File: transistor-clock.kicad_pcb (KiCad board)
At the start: 2 copper layers, 98 parts, among them J1 Screw_Terminal_01x02, J10 Conn_01x10_Socket, J11 Conn_01x06_Socket, J12 Conn_01x10_Socket, J13 Conn_01x03_Socket, J2 Conn_01x01_Socket, J3 Conn_01x01_Socket, J4 Conn_01x01_Socket, J5 Conn_01x01_Socket, J6 Conn_01x01_Socket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

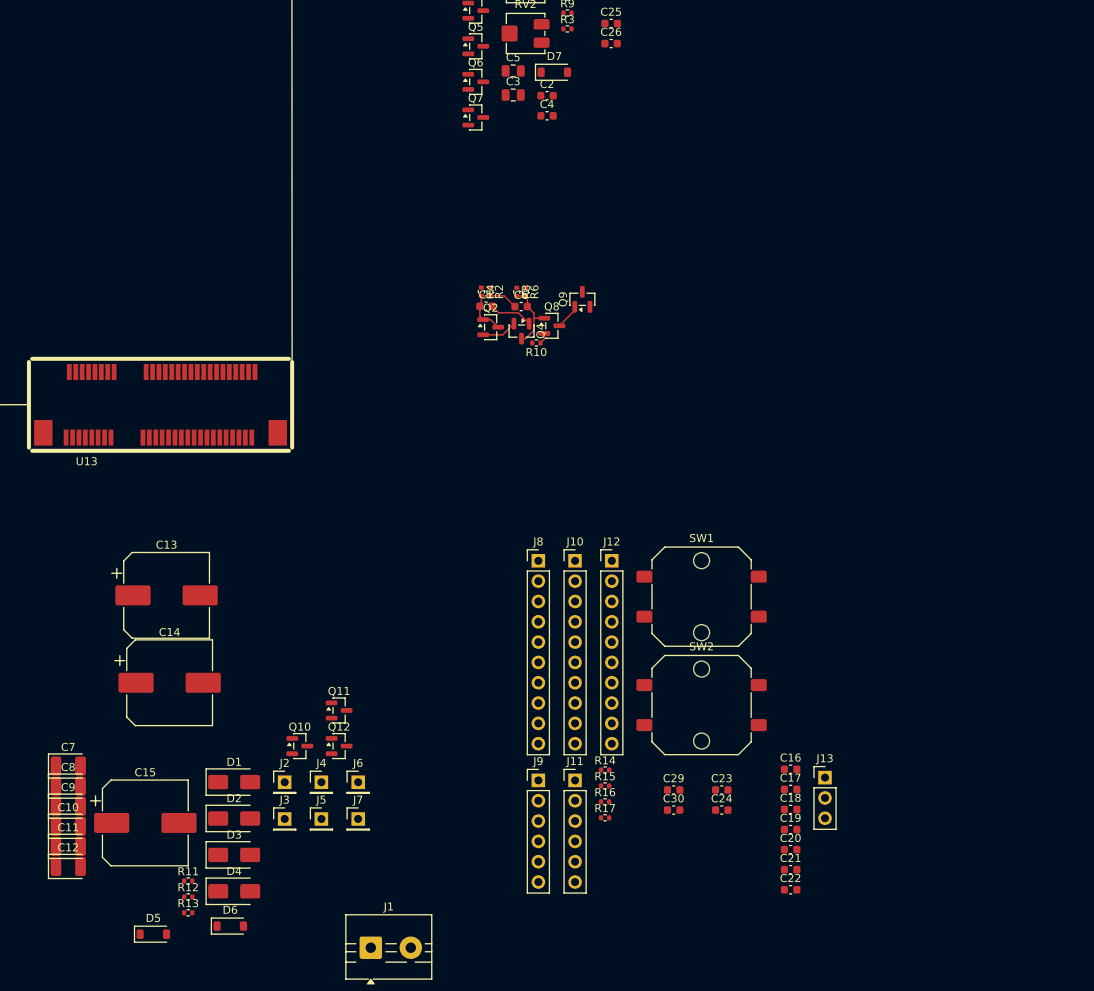
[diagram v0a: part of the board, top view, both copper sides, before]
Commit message: added module for PSU
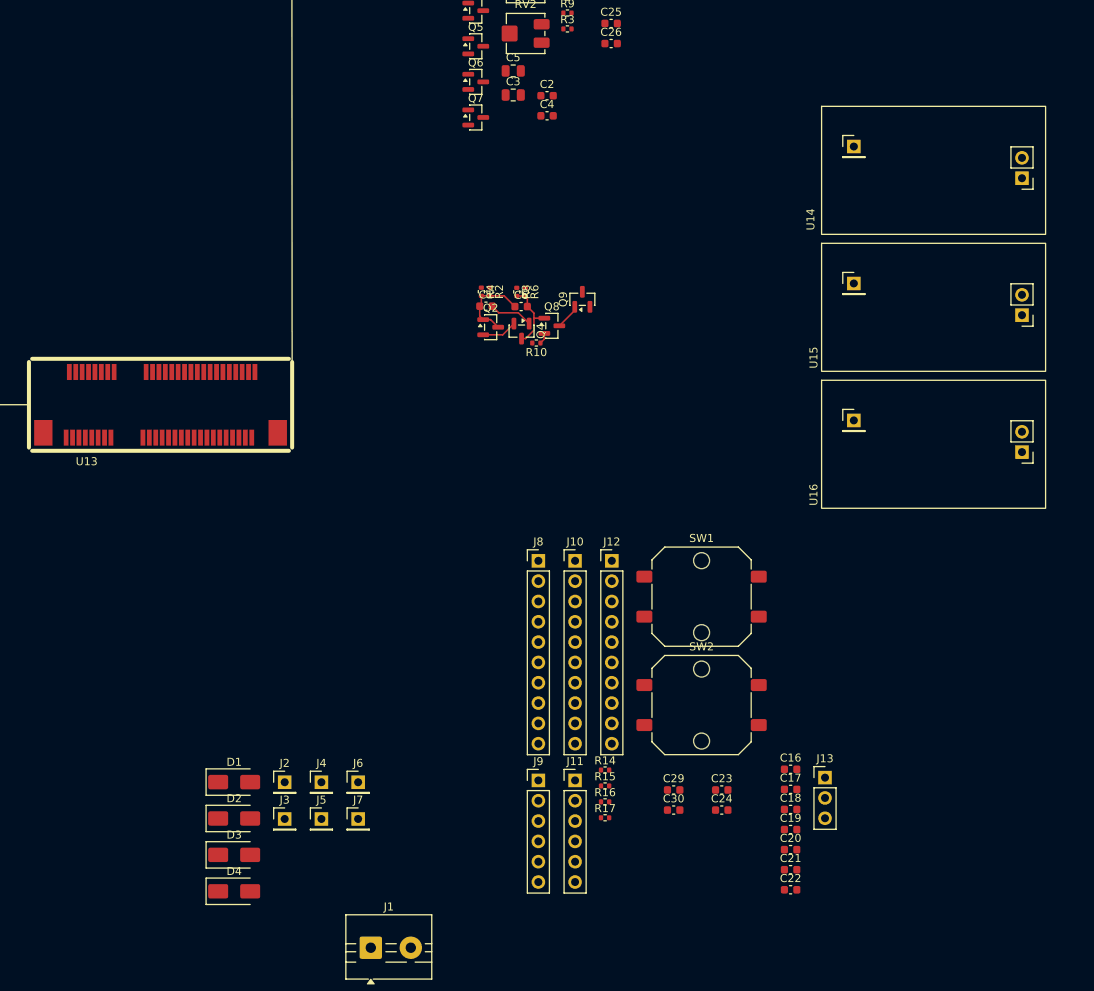
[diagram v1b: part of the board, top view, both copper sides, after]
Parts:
- removed C10, C11, C12, C7, C8, C9: 100u, Capacitor_Tantalum_SMD:CP_EIA-3528-12_Kemet-T
- removed C13, C14, C15: 1000u, Capacitor_SMD:CP_Elec_10x10.5
- removed D5: 3V9, Diode_SMD:D_SOD-123
- removed D6, D7: 13V, Diode_SMD:D_SOD-123
- removed Q10, Q11, Q12: MMBT3904, Package_TO_SOT_SMD:SOT-23
- removed R11, R12, R13: 560, Resistor_SMD:R_0402_1005Metric
- added U14: 3V3, custom:module_PSU, F.Cu at (404.7, 281.4)
- added U15: 12V, custom:module_PSU, F.Cu at (404.7, 298.5)
- added U16: -12V, custom:module_PSU, F.Cu at (404.7, 315.6)
- U1, U2, U3: value ~ -> SSR
- U10, U4, U5, U6, U7: value ~ -> flipflop
- U11, U12, U13, U8, U9: value ~ -> bin-to-dec
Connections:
- D2 pad 1: VSS -> Net-(D2-K)
- D4 pad 2: VSS -> Net-(D2-K)

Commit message: some routing on main board
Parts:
- added TP1: TestPoint_2Pole, Connector_PinHeader_2.54mm:PinHeader_1x02_P2.54mm_Vertical, F.Cu at (78.3, 506.9)
- added TR1: DST-6-36, custom:DST-6-36, F.Cu at (41.3, 350.9)
- added TR2: CL2-20-12, custom:CL2-20-12, F.Cu at (103.0, 350.8)
- R1, R10, R14, R15, R16, R17, R2, R3, R4, R5, R6, R7, R8, R9: footprint Resistor_SMD:R_0402_1005Metric -> Resistor_SMD:R_0603_1608Metric
- SW1: value SW_Push -> MIN +; footprint Button_Switch_SMD:SW_Push_1P1T_NO_CK_PTS125Sx43PSMTR -> Button_Switch_SMD:SW_SPST_EVQPE1
- SW2: value SW_Push -> HR +; footprint Button_Switch_SMD:SW_Push_1P1T_NO_CK_PTS125Sx43PSMTR -> Button_Switch_SMD:SW_SPST_EVQPE1
- moved C27 698.8 mm to (362.8, 437.4)
- moved C28 698.8 mm to (362.8, 439.9)
- moved U14 389.9 mm to (28.9, 385.4)
- moved U4 374.7 mm to (365.0, 502.6)
- moved R1 372.9 mm to (71.3, 495.1), turned to 90 degrees
- moved R5 368.9 mm to (70.8, 486.0), turned to 90 degrees
- moved C29 366.8 mm to (14.0, 437.8)
- moved C30 366.8 mm to (14.0, 440.3)
- moved R3 366.3 mm to (70.8, 489.8), turned to -90 degrees
- moved RV1 366.1 mm to (75.8, 496.2), turned to 180 degrees
- moved R9 362.6 mm to (80.3, 493.7), turned to -90 degrees
- moved R7 362.3 mm to (71.8, 480.6), turned to -90 degrees
- moved C2 357.9 mm to (72.4, 489.8), turned to 90 degrees
- moved Q1 356.8 mm to (77.2, 489.8), turned to 90 degrees
- moved U15 355.8 mm to (59.7, 385.4)
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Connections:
- C2 pad 1: Net-(Q1-B) -> Net-(Q1-C)
- C3 pad 1: Net-(Q1-B) -> Net-(Q1-C)
- Q1 pad 3: Net-(Q1-B) -> Net-(Q1-C)
- R1 pad 2: Net-(Q1-B) -> Net-(Q1-C)
- R3 pad 2: Net-(Q1-B) -> Net-(Q1-C)
- U8 pad 34: /counters/BCD_s0/Q1 -> /counters/BCD_m1/Q2
- U8 pad 36: /counters/BCD_s0/Q3 -> /counters/BCD_m1/Q1
- U8 pad 38: /counters/BCD_s0/Q3 -> /counters/BCD_m1/Q1
- U9 pad 12: /counters/BCD_m1/Q2 -> /counters/BCD_s1/Q2
- U9 pad 14: /counters/BCD_m1/Q1 -> /counters/BCD_s1/Q1
- U9 pad 16: /counters/BCD_m1/Q1 -> /counters/BCD_s1/Q1
- U9 pad 26: /counters/BCD_s1/Q2 -> /counters/BCD_s0/Q1
- U9 pad 28: /counters/BCD_s1/Q1 -> /counters/BCD_s0/Q3
- U9 pad 30: /counters/BCD_s1/Q1 -> /counters/BCD_s0/Q3
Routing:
- net /counters/BCD_h1/Q0: track 0.00 -> 496.8 mm, vias 0 -> 5
- net /counters/BCD_h0/Clr: track 0.00 -> 468.5 mm, vias 0 -> 4
- net /counters/BCD_h1/Clr: track 0.00 -> 360.6 mm, vias 0 -> 2
- net /counters/BCD_h0/Q3: track 0.00 -> 288.2 mm, vias 0 -> 5
- net /counters/BCD_h0/Q1: track 0.00 -> 244.5 mm, vias 0 -> 12
- net /counters/BCD_s0/Q1: track 0.00 -> 238.1 mm, vias 0 -> 14
- net /counters/BCD_m0/Q1: track 0.00 -> 231.8 mm, vias 0 -> 11
- net /counters/BCD_s0/Q0: track 0.00 -> 197.6 mm, vias 0 -> 12
- net /counters/BCD_s0/Q3: track 0.00 -> 197.6 mm, vias 0 -> 6
- net /counters/BCD_m0/Q0: track 0.00 -> 192.8 mm, vias 0 -> 12
- net /counters/BCD_m0/Q3: track 0.00 -> 182.1 mm, vias 0 -> 6
- net /Clk: track 0.00 -> 178.1 mm
- net /counters/BCD_h0/\Q0: track 0.00 -> 178.0 mm, vias 0 -> 12
- net /counters/BCD_s0/\Q0: track 0.00 -> 173.8 mm, vias 0 -> 10
- net /counters/BCD_m0/\Q0: track 0.00 -> 173.8 mm, vias 0 -> 10
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
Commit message: routy mcRouteface
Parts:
- TR1: value DST-6-36 -> Val**
- TR2: value CL2-20-12 -> Val**
- moved U7 447.1 mm to (419.5, 292.1), turned to 180 degrees
- moved J1 425.9 mm to (435.7, 474.3), turned to 180 degrees
- moved C30 425.3 mm to (430.5, 354.4), turned to 180 degrees
- moved C29 424.3 mm to (430.5, 356.9), turned to 180 degrees
- moved C22 423.1 mm to (40.1, 289.8), turned to 180 degrees
- moved U13 414.9 mm to (429.5, 388.6), turned to 90 degrees
- moved U14 387.4 mm to (415.6, 409.3), turned to 180 degrees
- moved C18 381.3 mm to (379.6, 289.7), turned to 180 degrees
- moved TR1 373.6 mm to (403.2, 443.8), turned to 90 degrees
- moved TP1 361.8 mm to (366.2, 287.8), turned to 90 degrees
- moved R1 359.6 mm to (373.2, 299.6), turned to -90 degrees
- moved R3 354.9 mm to (373.8, 304.9), turned to 90 degrees
- moved U4 354.7 mm to (79.5, 292.1), turned to 180 degrees
- moved RV1 353.5 mm to (368.7, 298.5), turned to 0 degrees
- moved C2 352.2 mm to (372.1, 304.9), turned to -90 degrees
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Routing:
- net Net-(U3-Pad12): track 0.00 -> 314.2 mm, vias 0 -> 3
- net Net-(R15-Pad1): track 16.6 -> 287.8 mm
- net Net-(R17-Pad1): track 17.1 -> 275.5 mm
- net /Sqr1: track 0.00 -> 248.0 mm
- net /counters/BDC_s0/8: track 5.53 -> 229.9 mm, vias 0 -> 3
- net /counters/BDC_s0/9: track 0.00 -> 219.5 mm, vias 0 -> 3
- net /counters/BDC_s0/7: track 14.8 -> 218.3 mm, vias 0 -> 2
- net +3V3: track 0.00 -> 203.5 mm, vias 0 -> 69
- net /counters/BDC_s0/4: track 26.3 -> 224.2 mm, vias 0 -> 1
- net /counters/BDC_s0/3: track 22.8 -> 218.2 mm, vias 0 -> 1
- net /counters/BDC_s0/2: track 19.6 -> 214.9 mm, vias 0 -> 1
- net /counters/BDC_s0/5: track 23.4 -> 218.0 mm, vias 0 -> 1
- net /counters/BDC_s0/6: track 19.2 -> 213.0 mm, vias 0 -> 1
- net /counters/BDC_s0/1: track 19.6 -> 206.7 mm, vias 0 -> 1
- net /counters/BDC_s0/0: track 11.9 -> 196.4 mm, vias 0 -> 1
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- added copper zone on B.Cu, net +3V3
- added copper zone on F.Cu, net GND
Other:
- board outline added: 430 x 210 mm

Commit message: routing
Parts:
- TR1: value Val** -> DST-6-36
- TR2: value Val** -> CL2-20-12
- moved U14 93.7 mm to (322.0, 412.3), turned to 90 degrees
- moved Q2 87.7 mm to (406.7, 403.5), turned to 180 degrees
- moved C1 85.7 mm to (407.3, 406.1), turned to 180 degrees
- moved Q4 84.4 mm to (402.9, 403.0), turned to 90 degrees
- moved R4 84.3 mm to (408.2, 408.6), turned to 90 degrees
- moved R10 84.3 mm to (400.6, 401.2), turned to 0 degrees
- moved R2 82.3 mm to (406.4, 408.6), turned to 90 degrees
- moved C6 81.3 mm to (402.9, 406.1), turned to 180 degrees
- moved Q8 80.2 mm to (399.1, 403.7), turned to 180 degrees
- moved U16 79.9 mm to (425.4, 407.9), turned to 0 degrees
- moved R8 79.7 mm to (403.8, 408.6), turned to 90 degrees
- moved R6 77.8 mm to (401.9, 408.6), turned to 90 degrees
- moved Q7 76.8 mm to (394.4, 408.6)
- moved Q9 76.8 mm to (399.0, 407.5)
- moved U3 63.9 mm to (51.4, 414.7), turned to 180 degrees
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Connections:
- TR2 pad 12: VSS -> Net-(Q9-E)
- TR2 pad 7: Net-(Q9-E) -> VSS
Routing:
- net /Sqr2: track 0.00 -> 364.3 mm
- net GND: track 63.0 -> 346.2 mm
- net /counters/relays_s0/Out3: track 0.00 -> 186.7 mm, vias 0 -> 1
- net /counters/relays_s0/Out2: track 0.00 -> 186.1 mm, vias 0 -> 1
- net /counters/relays_s0/Out1: track 0.00 -> 184.7 mm, vias 0 -> 1
- net /counters/relays_s0/Out0: track 0.00 -> 177.0 mm
- net /counters/relays_s0/Out7: track 0.00 -> 176.7 mm, vias 0 -> 1
- net /counters/relays_s0/Out4: track 0.00 -> 176.6 mm, vias 0 -> 1
- net /counters/relays_s0/Out8: track 0.00 -> 176.5 mm, vias 0 -> 1
- net /counters/relays_s0/Out5: track 0.00 -> 176.5 mm, vias 0 -> 1
- net /counters/relays_s0/Out6: track 0.00 -> 175.8 mm, vias 0 -> 1
- net /counters/relays_s0/Out9: track 0.00 -> 172.7 mm
- net VSS: track 51.5 -> 178.7 mm, vias 0 -> 2
- net /counters/relays_s1/Out5: track 0.00 -> 123.6 mm
- net /counters/relays_s1/Out3: track 0.00 -> 123.2 mm
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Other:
- board size 430 x 210 mm -> 430 x 170 mm

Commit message: flipflop wip
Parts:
- added F1: 250mA?, Fuse:Fuse_Littelfuse-NANO2-885, F.Cu at (398.9, 437.6)
- added F2: 2A?, Fuse:Fuse_Littelfuse-NANO2-885, F.Cu at (332.1, 396.5)
- added F3: 250mA?, Fuse:Fuse_Littelfuse-NANO2-885, F.Cu at (405.8, 423.0)
- added F4: 250mA?, Fuse:Fuse_Littelfuse-NANO2-885, F.Cu at (396.7, 423.0)
- added H1: MountingHole, MountingHole:MountingHole_4.3mm_M4_DIN965, F.Cu at (15.0, 285.0)
- added H2: MountingHole, MountingHole:MountingHole_4.3mm_M4_DIN965, F.Cu at (435.0, 285.0)
- added H3: MountingHole, MountingHole:MountingHole_4.3mm_M4_DIN965, F.Cu at (15.0, 447.0)
- added H4: MountingHole, MountingHole:MountingHole_4.3mm_M4_DIN965, F.Cu at (435.0, 447.0)
- added H5: MountingHole, MountingHole:MountingHole_4.3mm_M4_DIN965, F.Cu at (194.0, 335.0)
- added H6: MountingHole, MountingHole:MountingHole_4.3mm_M4_DIN965, F.Cu at (275.0, 335.0)
- moved D2 68.9 mm to (327.1, 434.7), turned to 90 degrees
- moved D1 61.8 mm to (332.9, 432.7), turned to 0 degrees
- moved D4 60.2 mm to (332.9, 436.7), turned to 180 degrees
- moved D3 53.0 mm to (338.9, 434.7), turned to -90 degrees
- moved J10 14.1 mm to (272.3, 445.0)
- moved J11 14.1 mm to (195.5, 445.0)
- moved J12 14.1 mm to (128.9, 445.0)
- moved J13 14.1 mm to (48.4, 445.0)
- moved J2 14.1 mm to (45.8, 450.0)
- moved J3 14.1 mm to (117.5, 450.0)
- moved J4 14.1 mm to (189.2, 450.0)
- moved J5 14.1 mm to (260.8, 450.0)
- moved J6 14.1 mm to (332.5, 450.0)
- moved J7 14.1 mm to (404.1, 450.0)
- moved J8 14.1 mm to (415.6, 445.0)
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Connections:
- net Net-(J1-Pin_1) renamed /AC_N
- net Net-(J13-Pin_1) renamed /counters/relays_h1/Out0
- net Net-(J13-Pin_2) renamed /counters/relays_h1/Out1
- net Net-(J13-Pin_3) renamed /counters/relays_h1/Out2
- TR1 pad 4: Net-(J1-Pin_2) -> /AC_L
- U14 pad 2: +3V3 -> Net-(U14-VCC)
- U15 pad 2: VDD -> Net-(U15-VCC)
- U16 pad 3: VSS -> Net-(U16-GND)
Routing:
- net Net-(J1-Pin_2): track 113.9 -> 27.3 mm
- net Net-(D2-K): track 42.1 -> 127.6 mm
- net Net-(D1-K): track 24.2 -> 87.0 mm, vias 0 -> 1
- net /AC_L: track 0.00 -> 60.0 mm
- net Net-(D3-A): track 40.1 -> 98.3 mm, vias 1 -> 0
- net Net-(U15-VCC): track 0.00 -> 47.6 mm
- net Net-(U16-GND): track 0.00 -> 42.9 mm
- net /counters/relays_m0/Out6: track 112.3 -> 143.0 mm
- net VDD: track 48.7 -> 21.9 mm
- net /counters/relays_h0/Out6: track 51.6 -> 73.9 mm
- net /counters/BDC_s1/5: track 178.5 -> 200.5 mm
- net /counters/relays_h0/Out5: track 51.6 -> 73.2 mm
- net /counters/relays_h0/Out7: track 51.6 -> 73.0 mm
- net /counters/relays_m1/Out3: track 61.0 -> 81.9 mm
- net /counters/relays_m1/Out2: track 61.0 -> 81.7 mm
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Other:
- board size 430 x 170 mm -> 430 x 172 mm

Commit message: updated production files
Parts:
- moved SW1 144.8 mm to (25.8, 447.6)
- moved SW2 144.8 mm to (25.7, 439.1)
- moved R7 33.3 mm to (358.9, 283.8), turned to 180 degrees
- moved R1 33.0 mm to (344.4, 283.3), turned to 0 degrees
- moved R5 33.0 mm to (353.5, 282.7), turned to 0 degrees
- moved R3 32.7 mm to (349.8, 282.7), turned to 180 degrees
- moved C4 30.7 mm to (353.5, 284.3), turned to 0 degrees
- moved C2 30.4 mm to (349.8, 284.3), turned to 0 degrees
- moved RV2 28.2 mm to (359.9, 288.1), turned to 90 degrees
- moved C5 28.0 mm to (353.6, 286.2), turned to 0 degrees
- moved C3 27.7 mm to (349.7, 286.2), turned to 0 degrees
- moved RV1 27.6 mm to (343.3, 287.7), turned to 90 degrees
- moved Q5 25.3 mm to (373.1, 287.9), turned to 0 degrees
- moved Q3 23.7 mm to (353.6, 289.3), turned to -90 degrees
- moved Q1 23.6 mm to (349.7, 289.1), turned to 0 degrees
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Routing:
- net Net-(R15-Pad1): track 287.8 -> 419.0 mm
- net Net-(R17-Pad1): track 275.5 -> 405.6 mm
- net GND: track 332.2 -> 378.7 mm
- net /Clk: track 167.1 -> 182.2 mm
- net Net-(Q3-C): track 20.7 -> 35.7 mm
- net Net-(C17-Pad1): track 121.1 -> 128.2 mm
- net Net-(C16-Pad1): track 144.5 -> 151.6 mm

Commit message: cleanup and DRC
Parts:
- added TP2: TestPoint_2Pole, Connector_PinHeader_2.54mm:PinHeader_1x02_P2.54mm_Vertical, F.Cu at (391.8, 405.1)
- moved H5 59.5 mm to (180.8, 393.0)
- moved H6 58.7 mm to (265.8, 393.0)
- moved C25 22.4 mm to (98.6, 348.1)
- moved C32 22.3 mm to (268.9, 350.7)
- moved C23 22.3 mm to (183.9, 348.1)
- moved C29 21.1 mm to (353.6, 350.7)
- moved C30 21.1 mm to (353.6, 348.1)
- moved C27 19.8 mm to (13.2, 350.7)
- moved C28 19.7 mm to (13.3, 348.1)
- moved C31 19.2 mm to (268.9, 348.1)
- moved C24 18.8 mm to (183.8, 350.7)
- moved C26 18.8 mm to (98.6, 350.7)
- moved J1 6.11 mm to (421.6, 440.8)
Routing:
- net /counters/BCD_m0/Q0: track 198.0 -> 182.6 mm
- net +3V3: track 206.3 -> 196.9 mm, vias 70 -> 67
- net /counters/BCD_s0/Q1: track 232.5 -> 224.9 mm, vias 14 -> 12
- net Net-(Q9-E): track 139.0 -> 145.2 mm
- net /counters/BCD_m0/Q3: track 183.6 -> 177.9 mm
- net /counters/BCD_s0/Q0: track 192.1 -> 187.1 mm
- net VSS: track 175.1 -> 179.9 mm
- net /AC_N: track 83.5 -> 78.8 mm
- net Net-(Q1-B): track 15.4 -> 11.0 mm
- net Net-(J1-Pin_2): track 27.3 -> 23.8 mm
- net /counters/BDC_m1/1: track 77.4 -> 73.9 mm
- net Net-(D1-A): track 126.4 -> 123.4 mm
- net /counters/BCD_s0/Clr: track 36.2 -> 33.9 mm
- net Net-(U3-Pad12): track 323.1 -> 321.3 mm
- net Net-(U12-Pad15): track 18.6 -> 17.3 mm
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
